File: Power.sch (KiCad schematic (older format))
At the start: 20 parts, among them J2 Conn_02x05_Odd_Even, U5 R-78E3.3-0.5, U6 LD2981ABU50TR

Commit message: Re-annotation.
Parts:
- renumbered C20 to C16, C21 to C17, C22 to C18, C23 to C19, C24 to C20, C25 to C21, C26 to C22, C27 to C23, C28 to C24, C29 to C25, R9 to R8, U5 to U4, U6 to U5
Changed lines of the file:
@@
 $Descr A4 11693 8268
 encoding utf-8
-Sheet 2 6
+Sheet 2 11
 Title ""
 Date ""
@@
 AR Path="/61C9E219" Ref="R?"  Part="1"
 AR Path="/61C5176D/61C9E219" Ref="R?"  Part="1"
-AR Path="/61C80AC7/61C9E219" Ref="R9"  Part="1"
-F 0 "R9" H 5470 2446 50  0000 L CNN
+AR Path="/61C80AC7/61C9E219" Ref="R8"  Part="1"
+F 0 "R8" H 5470 2446 50  0000 L CNN
 F 1 "1k" H 5470 2355 50  0000 L CNN
 F 2 "Resistor_SMD:R_0603_1608Metric" V 5330 2400 50  0001 C CNN
@@
 AR Path="/61C9E21F" Ref="#PWR?"  Part="1"
 AR Path="/61C5176D/61C9E21F" Ref="#PWR?"  Part="1"
-AR Path="/61C80AC7/61C9E21F" Ref="#PWR040"  Part="1"
-F 0 "#PWR040" H 6000 2150 50  0001 C CNN
+AR Path="/61C80AC7/61C9E21F" Ref="#PWR031"  Part="1"
+F 0 "#PWR031" H 6000 2150 50  0001 C CNN
 F 1 "GND" H 6005 2227 50  0000 C CNN
 F 2 "" H 6000 2400 50  0001 C CNN
@@
 AR Path="/61C9E253" Ref="#PWR?"  Part="1"
 AR Path="/61C5176D/61C9E253" Ref="#PWR?"  Part="1"
-AR Path="/61C80AC7/61C9E253" Ref="#PWR032"  Part="1"
-F 0 "#PWR032" H 2850 1850 50  0001 C CNN
+AR Path="/61C80AC7/61C9E253" Ref="#PWR023"  Part="1"
+F 0 "#PWR023" H 2850 1850 50  0001 C CNN
 F 1 "GND" H 2850 1950 50  0000 C CNN
 F 2 "" H 2850 2100 50  0001 C CNN
@@
 AR Path="/61C9E27E" Ref="C?"  Part="1"
 AR Path="/61C5176D/61C9E27E" Ref="C?"  Part="1"
-AR Path="/61C80AC7/61C9E27E" Ref="C23"  Part="1"
-F 0 "C23" H 3915 4796 50  0000 L CNN
+AR Path="/61C80AC7/61C9E27E" Ref="C19"  Part="1"
+F 0 "C19" H 3915 4796 50  0000 L CNN
 F 1 "100n" H 3915 4705 50  0000 L CNN
 F 2 "Capacitor_SMD:C_0402_1005Metric" H 3838 4600 50  0001 C CNN
@@
 AR Path="/61C9E289" Ref="C?"  Part="1"
 AR Path="/61C5176D/61C9E289" Ref="C?"  Part="1"
-AR Path="/61C80AC7/61C9E289" Ref="C27"  Part="1"
-F 0 "C27" H 5015 4796 50  0000 L CNN
+AR Path="/61C80AC7/61C9E289" Ref="C23"  Part="1"
+F 0 "C23" H 5015 4796 50  0000 L CNN
 F 1 "100n" H 5015 4705 50  0000 L CNN
 F 2 "Capacitor_SMD:C_0402_1005Metric" H 4938 4600 50  0001 C CNN
@@
 AR Path="/61C9E2C9" Ref="#PWR?"  Part="1"
 AR Path="/61C5176D/61C9E2C9" Ref="#PWR?"  Part="1"
-AR Path="/61C80AC7/61C9E2C9" Ref="#PWR035"  Part="1"
-F 0 "#PWR035" H 4350 4700 50  0001 C CNN
+AR Path="/61C80AC7/61C9E2C9" Ref="#PWR026"  Part="1"
+F 0 "#PWR026" H 4350 4700 50  0001 C CNN
 F 1 "GND" H 4355 4777 50  0000 C CNN
 F 2 "" H 4350 4950 50  0001 C CNN
@@
 AR Path="/61C9E2D7" Ref="#PWR?"  Part="1"
 AR Path="/61C5176D/61C9E2D7" Ref="#PWR?"  Part="1"
-AR Path="/61C80AC7/61C9E2D7" Ref="#PWR036"  Part="1"
-F 0 "#PWR036" H 5100 1550 50  0001 C CNN
+AR Path="/61C80AC7/61C9E2D7" Ref="#PWR027"  Part="1"
+F 0 "#PWR027" H 5100 1550 50  0001 C CNN
 F 1 "+12V" H 5100 1840 50  0000 C CNN
 F 2 "" H 5100 1700 50  0001 C CNN
@@
 AR Path="/61A5CA04" Ref="C?"  Part="1"
 AR Path="/61C5176D/61A5CA04" Ref="C?"  Part="1"
-AR Path="/61C80AC7/61A5CA04" Ref="C24"  Part="1"
-F 0 "C24" H 4965 1896 50  0000 L CNN
+AR Path="/61C80AC7/61A5CA04" Ref="C20"  Part="1"
+F 0 "C20" H 4965 1896 50  0000 L CNN
 F 1 "22u" H 4965 1805 50  0000 L CNN
 F 2 "Capacitor_SMD:C_1206_3216Metric" H 4888 1700 50  0001 C CNN
@@
 AR Path="/61A5D917" Ref="C?"  Part="1"
 AR Path="/61C5176D/61A5D917" Ref="C?"  Part="1"
-AR Path="/61C80AC7/61A5D917" Ref="C25"  Part="1"
-F 0 "C25" H 4965 2296 50  0000 L CNN
+AR Path="/61C80AC7/61A5D917" Ref="C21"  Part="1"
+F 0 "C21" H 4965 2296 50  0000 L CNN
 F 1 "22u" H 4965 2205 50  0000 L CNN
 F 2 "Capacitor_SMD:C_1206_3216Metric" H 4888 2100 50  0001 C CNN
@@
 	4300 1700 4400 1700
 $Comp
-L power:-12V #PWR037
+L power:-12V #PWR028
 U 1 1 61A6FD5E
 P 5100 2400
-F 0 "#PWR037" H 5100 2500 50  0001 C CNN
+F 0 "#PWR028" H 5100 2500 50  0001 C CNN
 F 1 "-12V" H 5115 2573 50  0000 C CNN
 F 2 "" H 5100 2400 50  0001 C CNN
@@
 AR Path="/61AE4D4E" Ref="C?"  Part="1"
 AR Path="/61C5176D/61AE4D4E" Ref="C?"  Part="1"
-AR Path="/61C80AC7/61AE4D4E" Ref="C29"  Part="1"
-F 0 "C29" H 5465 4796 50  0000 L CNN
+AR Path="/61C80AC7/61AE4D4E" Ref="C25"  Part="1"
+F 0 "C25" H 5465 4796 50  0000 L CNN
 F 1 "22u" H 5465 4705 50  0000 L CNN
 F 2 "Capacitor_SMD:C_1206_3216Metric" H 5388 4600 50  0001 C CNN
@@
 $EndComp
 $Comp
-L power:+3.3V #PWR038
+L power:+3.3V #PWR029
 U 1 1 61B17B4F
 P 5350 3350
-F 0 "#PWR038" H 5350 3200 50  0001 C CNN
+F 0 "#PWR029" H 5350 3200 50  0001 C CNN
 F 1 "+3.3V" H 5365 3523 50  0000 C CNN
 F 2 "" H 5350 3350 50  0001 C CNN
@@
 $EndComp
 $Comp
-L Device:C C21
+L Device:C C17
 U 1 1 61B18CC1
 P 3350 4750
-F 0 "C21" H 3465 4796 50  0000 L CNN
+F 0 "C17" H 3465 4796 50  0000 L CNN
 F 1 "4u7" H 3465 4705 50  0000 L CNN
 F 2 "Capacitor_SMD:C_0805_2012Metric" H 3388 4600 50  0001 C CNN
@@
 AR Path="/61D897BC" Ref="C?"  Part="1"
 AR Path="/61C5176D/61D897BC" Ref="C?"  Part="1"
-AR Path="/61C80AC7/61D897BC" Ref="C28"  Part="1"
-F 0 "C28" H 5465 3596 50  0000 L CNN
+AR Path="/61C80AC7/61D897BC" Ref="C24"  Part="1"
+F 0 "C24" H 5465 3596 50  0000 L CNN
 F 1 "22u" H 5465 3505 50  0000 L CNN
 F 2 "Capacitor_SMD:C_1206_3216Metric" H 5388 3400 50  0001 C CNN
@@
 AR Path="/61D89A8E" Ref="C?"  Part="1"
 AR Path="/61C5176D/61D89A8E" Ref="C?"  Part="1"
-AR Path="/61C80AC7/61D89A8E" Ref="C26"  Part="1"
-F 0 "C26" H 5015 3596 50  0000 L CNN
+AR Path="/61C80AC7/61D89A8E" Ref="C22"  Part="1"
+F 0 "C22" H 5015 3596 50  0000 L CNN
 F 1 "100n" H 5015 3505 50  0000 L CNN
 F 2 "Capacitor_SMD:C_0402_1005Metric" H 4938 3400 50  0001 C CNN
@@
 AR Path="/61D89A9D" Ref="C?"  Part="1"
 AR Path="/61C5176D/61D89A9D" Ref="C?"  Part="1"
-AR Path="/61C80AC7/61D89A9D" Ref="C22"  Part="1"
-F 0 "C22" H 3915 3596 50  0000 L CNN
+AR Path="/61C80AC7/61D89A9D" Ref="C18"  Part="1"
+F 0 "C18" H 3915 3596 50  0000 L CNN
 F 1 "100n" H 3915 3505 50  0000 L CNN
 F 2 "Capacitor_SMD:C_0402_1005Metric" H 3838 3400 50  0001 C CNN
@@
 AR Path="/61D89AAC" Ref="#PWR?"  Part="1"
 AR Path="/61C5176D/61D89AAC" Ref="#PWR?"  Part="1"
-AR Path="/61C80AC7/61D89AAC" Ref="#PWR034"  Part="1"
-F 0 "#PWR034" H 4350 3500 50  0001 C CNN
+AR Path="/61C80AC7/61D89AAC" Ref="#PWR025"  Part="1"
+F 0 "#PWR025" H 4350 3500 50  0001 C CNN
 F 1 "GND" H 4355 3577 50  0000 C CNN
 F 2 "" H 4350 3750 50  0001 C CNN
@@
 AR Path="/61D89ACC" Ref="#PWR?"  Part="1"
 AR Path="/61C5176D/61D89ACC" Ref="#PWR?"  Part="1"
-AR Path="/61C80AC7/61D89ACC" Ref="#PWR031"  Part="1"
-F 0 "#PWR031" H 2650 3200 50  0001 C CNN
+AR Path="/61C80AC7/61D89ACC" Ref="#PWR022"  Part="1"
+F 0 "#PWR022" H 2650 3200 50  0001 C CNN
 F 1 "+12V" H 2650 3490 50  0000 C CNN
 F 2 "" H 2650 3350 50  0001 C CNN
@@
 $EndComp
 $Comp
-L Device:C C20
+L Device:C C16
 U 1 1 61D89AD6
 P 3350 3550
-F 0 "C20" H 3465 3596 50  0000 L CNN
+F 0 "C16" H 3465 3596 50  0000 L CNN
 F 1 "4u7" H 3465 3505 50  0000 L CNN
 F 2 "Capacitor_SMD:C_0805_2012Metric" H 3388 3400 50  0001 C CNN
@@
 $EndComp
 $Comp
-L Regulator_Switching:R-78E3.3-0.5 U5
+L Regulator_Switching:R-78E3.3-0.5 U4
 U 1 1 61D8F6E2
 P 4350 3350
-F 0 "U5" H 4350 3592 50  0000 C CNN
+F 0 "U4" H 4350 3592 50  0000 C CNN
 F 1 "R-78E3.3-0.5" H 4350 3501 50  0000 C CNN
 F 2 "Converter_DCDC:Converter_DCDC_RECOM_R-78E-0.5_THT" H 4400 3100 50  0001 L CIN
@@
 Connection ~ 5350 3350
 $Comp
-L power:+5V #PWR039
+L power:+5V #PWR030
 U 1 1 61AB9C33
 P 5350 4550
-F 0 "#PWR039" H 5350 4400 50  0001 C CNN
+F 0 "#PWR030" H 5350 4400 50  0001 C CNN
 F 1 "+5V" H 5365 4723 50  0000 C CNN
 F 2 "" H 5350 4550 50  0001 C CNN
@@
 AR Path="/61ACBF55" Ref="#PWR?"  Part="1"
 AR Path="/61C5176D/61ACBF55" Ref="#PWR?"  Part="1"
-AR Path="/61C80AC7/61ACBF55" Ref="#PWR033"  Part="1"
-F 0 "#PWR033" H 3350 4400 50  0001 C CNN
+AR Path="/61C80AC7/61ACBF55" Ref="#PWR024"  Part="1"
+F 0 "#PWR024" H 3350 4400 50  0001 C CNN
 F 1 "+12V" H 3350 4690 50  0000 C CNN
 F 2 "" H 3350 4550 50  0001 C CNN
@@
 Connection ~ 3350 4550
 $Comp
-L LD2981:LD2981ABU50TR U6
+L LD2981:LD2981ABU50TR U5
 U 1 1 61AD1D02
 P 4350 4550
-F 0 "U6" H 4350 4792 50  0000 C CNN
+F 0 "U5" H 4350 4792 50  0000 C CNN
 F 1 "LD2981ABU50TR" H 4350 4701 50  0000 C CNN
 F 2 "Package_TO_SOT_SMD:SOT-89-3" H 4350 4750 50  0001 C CIN

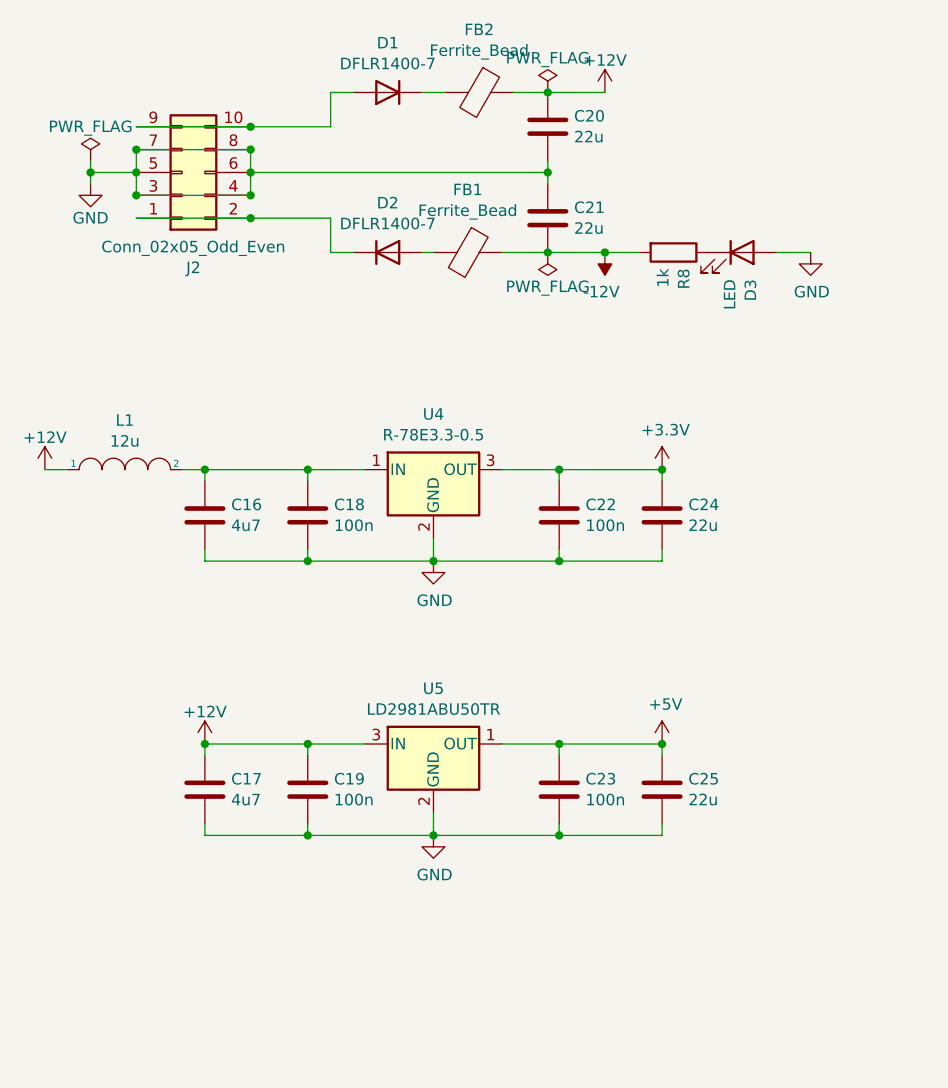
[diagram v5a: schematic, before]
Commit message: Assigned pins and cleared schema rules.
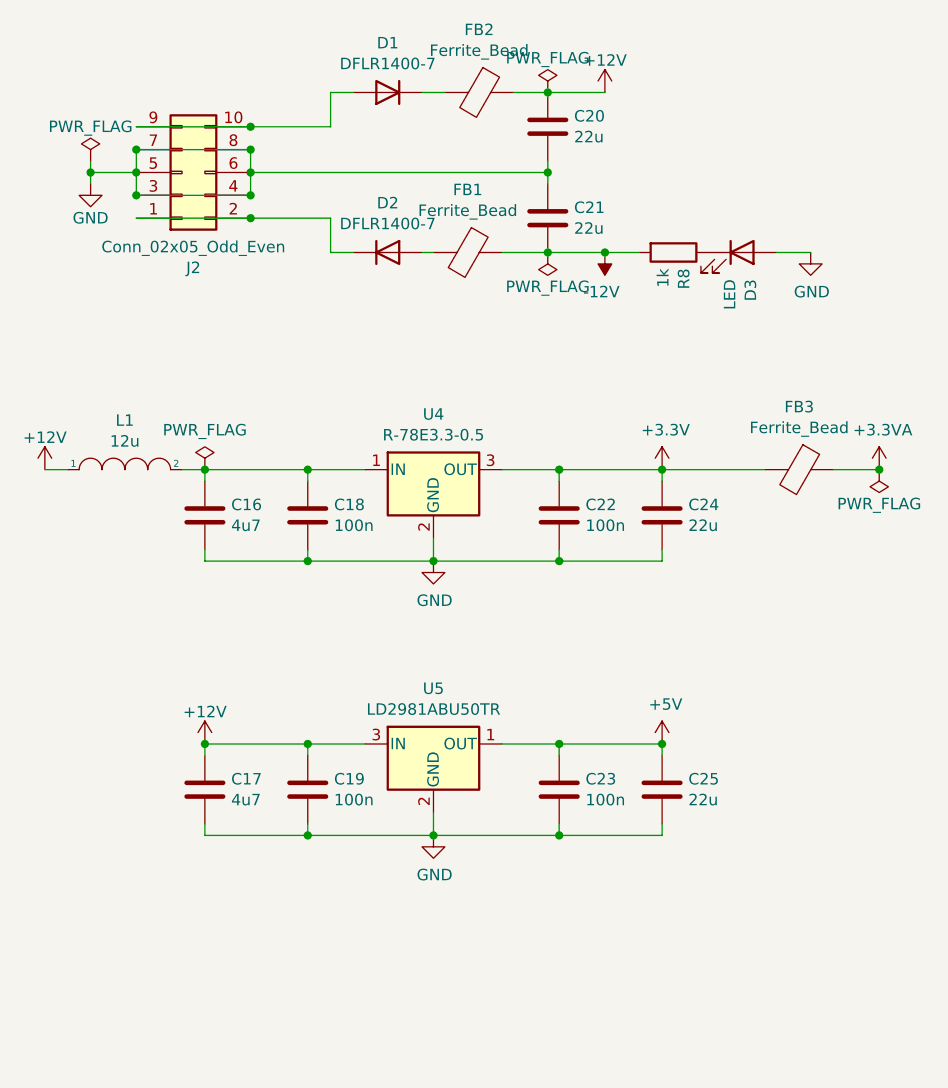
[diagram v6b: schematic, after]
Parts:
- added FB3: Ferrite_Bead, Inductor_SMD:L_0603_1608Metric, symbol Device:Ferrite_Bead
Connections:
- net +3V3: now also FB3.2
- new net +3.3VA: FB3.1
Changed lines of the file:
@@
 AR Path="/61C9E1F6" Ref="#FLG?"  Part="1"
 AR Path="/61C5176D/61C9E1F6" Ref="#FLG?"  Part="1"
-AR Path="/61C80AC7/61C9E1F6" Ref="#FLG02"  Part="1"
-F 0 "#FLG02" H 4850 1775 50  0001 C CNN
+AR Path="/61C80AC7/61C9E1F6" Ref="#FLG03"  Part="1"
+F 0 "#FLG03" H 4850 1775 50  0001 C CNN
 F 1 "PWR_FLAG" H 4850 1850 50  0000 C CNN
 F 2 "" H 4850 1700 50  0001 C CNN
@@
 AR Path="/61C9E1FC" Ref="#FLG?"  Part="1"
 AR Path="/61C5176D/61C9E1FC" Ref="#FLG?"  Part="1"
-AR Path="/61C80AC7/61C9E1FC" Ref="#FLG03"  Part="1"
-F 0 "#FLG03" H 4850 2475 50  0001 C CNN
+AR Path="/61C80AC7/61C9E1FC" Ref="#FLG04"  Part="1"
+F 0 "#FLG04" H 4850 2475 50  0001 C CNN
 F 1 "PWR_FLAG" H 4850 2550 50  0000 C CNN
 F 2 "" H 4850 2400 50  0001 C CNN
@@
 AR Path="/61C9E21F" Ref="#PWR?"  Part="1"
 AR Path="/61C5176D/61C9E21F" Ref="#PWR?"  Part="1"
-AR Path="/61C80AC7/61C9E21F" Ref="#PWR031"  Part="1"
-F 0 "#PWR031" H 6000 2150 50  0001 C CNN
+AR Path="/61C80AC7/61C9E21F" Ref="#PWR032"  Part="1"
+F 0 "#PWR032" H 6000 2150 50  0001 C CNN
 F 1 "GND" H 6005 2227 50  0000 C CNN
 F 2 "" H 6000 2400 50  0001 C CNN
@@
 AR Path="/61C9E253" Ref="#PWR?"  Part="1"
 AR Path="/61C5176D/61C9E253" Ref="#PWR?"  Part="1"
-AR Path="/61C80AC7/61C9E253" Ref="#PWR023"  Part="1"
-F 0 "#PWR023" H 2850 1850 50  0001 C CNN
+AR Path="/61C80AC7/61C9E253" Ref="#PWR024"  Part="1"
+F 0 "#PWR024" H 2850 1850 50  0001 C CNN
 F 1 "GND" H 2850 1950 50  0000 C CNN
 F 2 "" H 2850 2100 50  0001 C CNN
@@
 AR Path="/61C9E2C9" Ref="#PWR?"  Part="1"
 AR Path="/61C5176D/61C9E2C9" Ref="#PWR?"  Part="1"
-AR Path="/61C80AC7/61C9E2C9" Ref="#PWR026"  Part="1"
-F 0 "#PWR026" H 4350 4700 50  0001 C CNN
+AR Path="/61C80AC7/61C9E2C9" Ref="#PWR027"  Part="1"
+F 0 "#PWR027" H 4350 4700 50  0001 C CNN
 F 1 "GND" H 4355 4777 50  0000 C CNN
 F 2 "" H 4350 4950 50  0001 C CNN
@@
 AR Path="/61C9E2D7" Ref="#PWR?"  Part="1"
 AR Path="/61C5176D/61C9E2D7" Ref="#PWR?"  Part="1"
-AR Path="/61C80AC7/61C9E2D7" Ref="#PWR027"  Part="1"
-F 0 "#PWR027" H 5100 1550 50  0001 C CNN
+AR Path="/61C80AC7/61C9E2D7" Ref="#PWR028"  Part="1"
+F 0 "#PWR028" H 5100 1550 50  0001 C CNN
 F 1 "+12V" H 5100 1840 50  0000 C CNN
 F 2 "" H 5100 1700 50  0001 C CNN
@@
 	4300 1700 4400 1700
 $Comp
-L power:-12V #PWR028
+L power:-12V #PWR029
 U 1 1 61A6FD5E
 P 5100 2400
-F 0 "#PWR028" H 5100 2500 50  0001 C CNN
+F 0 "#PWR029" H 5100 2500 50  0001 C CNN
 F 1 "-12V" H 5115 2573 50  0000 C CNN
 F 2 "" H 5100 2400 50  0001 C CNN
@@
 $EndComp
 $Comp
-L power:+3.3V #PWR029
+L power:+3.3V #PWR030
 U 1 1 61B17B4F
 P 5350 3350
-F 0 "#PWR029" H 5350 3200 50  0001 C CNN
+F 0 "#PWR030" H 5350 3200 50  0001 C CNN
 F 1 "+3.3V" H 5365 3523 50  0000 C CNN
 F 2 "" H 5350 3350 50  0001 C CNN
@@
 	3800 3400 3800 3350
 Wire Wire Line
-	3800 3350 4050 3350
-Wire Wire Line
 	3800 3700 3800 3750
 Wire Wire Line
 	3800 3750 4350 3750
-Connection ~ 3800 3350
 $Comp
 L Device:C C?
@@
 AR Path="/61D89AAC" Ref="#PWR?"  Part="1"
 AR Path="/61C5176D/61D89AAC" Ref="#PWR?"  Part="1"
-AR Path="/61C80AC7/61D89AAC" Ref="#PWR025"  Part="1"
-F 0 "#PWR025" H 4350 3500 50  0001 C CNN
+AR Path="/61C80AC7/61D89AAC" Ref="#PWR026"  Part="1"
+F 0 "#PWR026" H 4350 3500 50  0001 C CNN
 F 1 "GND" H 4355 3577 50  0000 C CNN
 F 2 "" H 4350 3750 50  0001 C CNN
@@
 AR Path="/61D89ACC" Ref="#PWR?"  Part="1"
 AR Path="/61C5176D/61D89ACC" Ref="#PWR?"  Part="1"
-AR Path="/61C80AC7/61D89ACC" Ref="#PWR022"  Part="1"
-F 0 "#PWR022" H 2650 3200 50  0001 C CNN
+AR Path="/61C80AC7/61D89ACC" Ref="#PWR023"  Part="1"
+F 0 "#PWR023" H 2650 3200 50  0001 C CNN
 F 1 "+12V" H 2650 3490 50  0000 C CNN
 F 2 "" H 2650 3350 50  0001 C CNN
@@
 Connection ~ 5350 3350
 $Comp
-L power:+5V #PWR030
+L power:+5V #PWR031
 U 1 1 61AB9C33
 P 5350 4550
-F 0 "#PWR030" H 5350 4400 50  0001 C CNN
+F 0 "#PWR031" H 5350 4400 50  0001 C CNN
 F 1 "+5V" H 5365 4723 50  0000 C CNN
 F 2 "" H 5350 4550 50  0001 C CNN
@@
 AR Path="/61ACBF55" Ref="#PWR?"  Part="1"
 AR Path="/61C5176D/61ACBF55" Ref="#PWR?"  Part="1"
-AR Path="/61C80AC7/61ACBF55" Ref="#PWR024"  Part="1"
-F 0 "#PWR024" H 3350 4400 50  0001 C CNN
+AR Path="/61C80AC7/61ACBF55" Ref="#PWR025"  Part="1"
+F 0 "#PWR025" H 3350 4400 50  0001 C CNN
 F 1 "+12V" H 3350 4690 50  0000 C CNN
 F 2 "" H 3350 4550 50  0001 C CNN
@@
 	1    0    0    -1
 $EndComp
+Wire Wire Line
+	3800 3350 4050 3350
+Connection ~ 3800 3350
+$Comp
+L power:PWR_FLAG #FLG02
+U 1 1 62543E2F
+P 3350 3350
+F 0 "#FLG02" H 3350 3425 50  0001 C CNN
+F 1 "PWR_FLAG" H 3350 3523 50  0000 C CNN
+F 2 "" H 3350 3350 50  0001 C CNN
+F 3 "~" H 3350 3350 50  0001 C CNN
+	1    3350 3350
+	1    0    0    -1
+$EndComp
+$Comp
+L Device:Ferrite_Bead FB?
+U 1 1 62569985
+P 5950 3350
+AR Path="/5F2EFD7F/62569985" Ref="FB?"  Part="1"
+AR Path="/62569985" Ref="FB?"  Part="1"
+AR Path="/61C5176D/62569985" Ref="FB?"  Part="1"
+AR Path="/61C80AC7/62569985" Ref="FB3"  Part="1"
+F 0 "FB3" V 5676 3350 50  0000 C CNN
+F 1 "Ferrite_Bead" V 5767 3350 50  0000 C CNN
+F 2 "Inductor_SMD:L_0603_1608Metric" V 5880 3350 50  0001 C CNN
+F 3 "~" H 5950 3350 50  0001 C CNN
+	1    5950 3350
+	0    1    1    0
+$EndComp
+Wire Wire Line
+	5350 3350 5800 3350
+$Comp
+L power:+3.3VA #PWR033
+U 1 1 6256DC54
+P 6300 3350
+F 0 "#PWR033" H 6300 3200 50  0001 C CNN
+F 1 "+3.3VA" H 6315 3523 50  0000 C CNN
+F 2 "" H 6300 3350 50  0001 C CNN
+F 3 "" H 6300 3350 50  0001 C CNN
+	1    6300 3350
+	1    0    0    -1
+$EndComp
+Wire Wire Line
+	6100 3350 6300 3350
+$Comp
+L power:PWR_FLAG #FLG?
+U 1 1 625C7790
+P 6300 3350
+AR Path="/5F2EFD7F/625C7790" Ref="#FLG?"  Part="1"
+AR Path="/625C7790" Ref="#FLG?"  Part="1"
+AR Path="/61C5176D/625C7790" Ref="#FLG?"  Part="1"
+AR Path="/61C80AC7/625C7790" Ref="#FLG05"  Part="1"
+F 0 "#FLG05" H 6300 3425 50  0001 C CNN
+F 1 "PWR_FLAG" H 6300 3500 50  0000 C CNN
+F 2 "" H 6300 3350 50  0001 C CNN
+F 3 "" H 6300 3350 50  0001 C CNN
+	1    6300 3350
+	-1   0    0    1
+$EndComp
+Connection ~ 6300 3350
 $EndSCHEMATC
